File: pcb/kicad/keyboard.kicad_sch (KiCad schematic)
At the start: 0 parts

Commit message: pcb: make net-map the project schematic (keyboard.kicad_sch)
Rename net-map.kicad_sch -> keyboard.kicad_sch so it opens inside
keyboard.kicad_pro as the project's schematic (KiCad auto-associates by
filename; reference project confirms sheets:[] is fine). Refresh the
viewable render at pcb/kicad/net-map.png. Title marks it an overview,
not a netlist source — the board stays schematic-less.
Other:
- title: Atlas — Net Map -> Atlas — Net Map (overview, not netlist source)
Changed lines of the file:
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@@
 	(paper "A3")
 	(title_block
-		(title "Atlas — Net Map")
+		(title "Atlas — Net Map (overview, not netlist source)")
 		(date "2026-06-13")
-		(rev "v1")
+		(rev "v2")
 		(company "mwlabs")
 	)

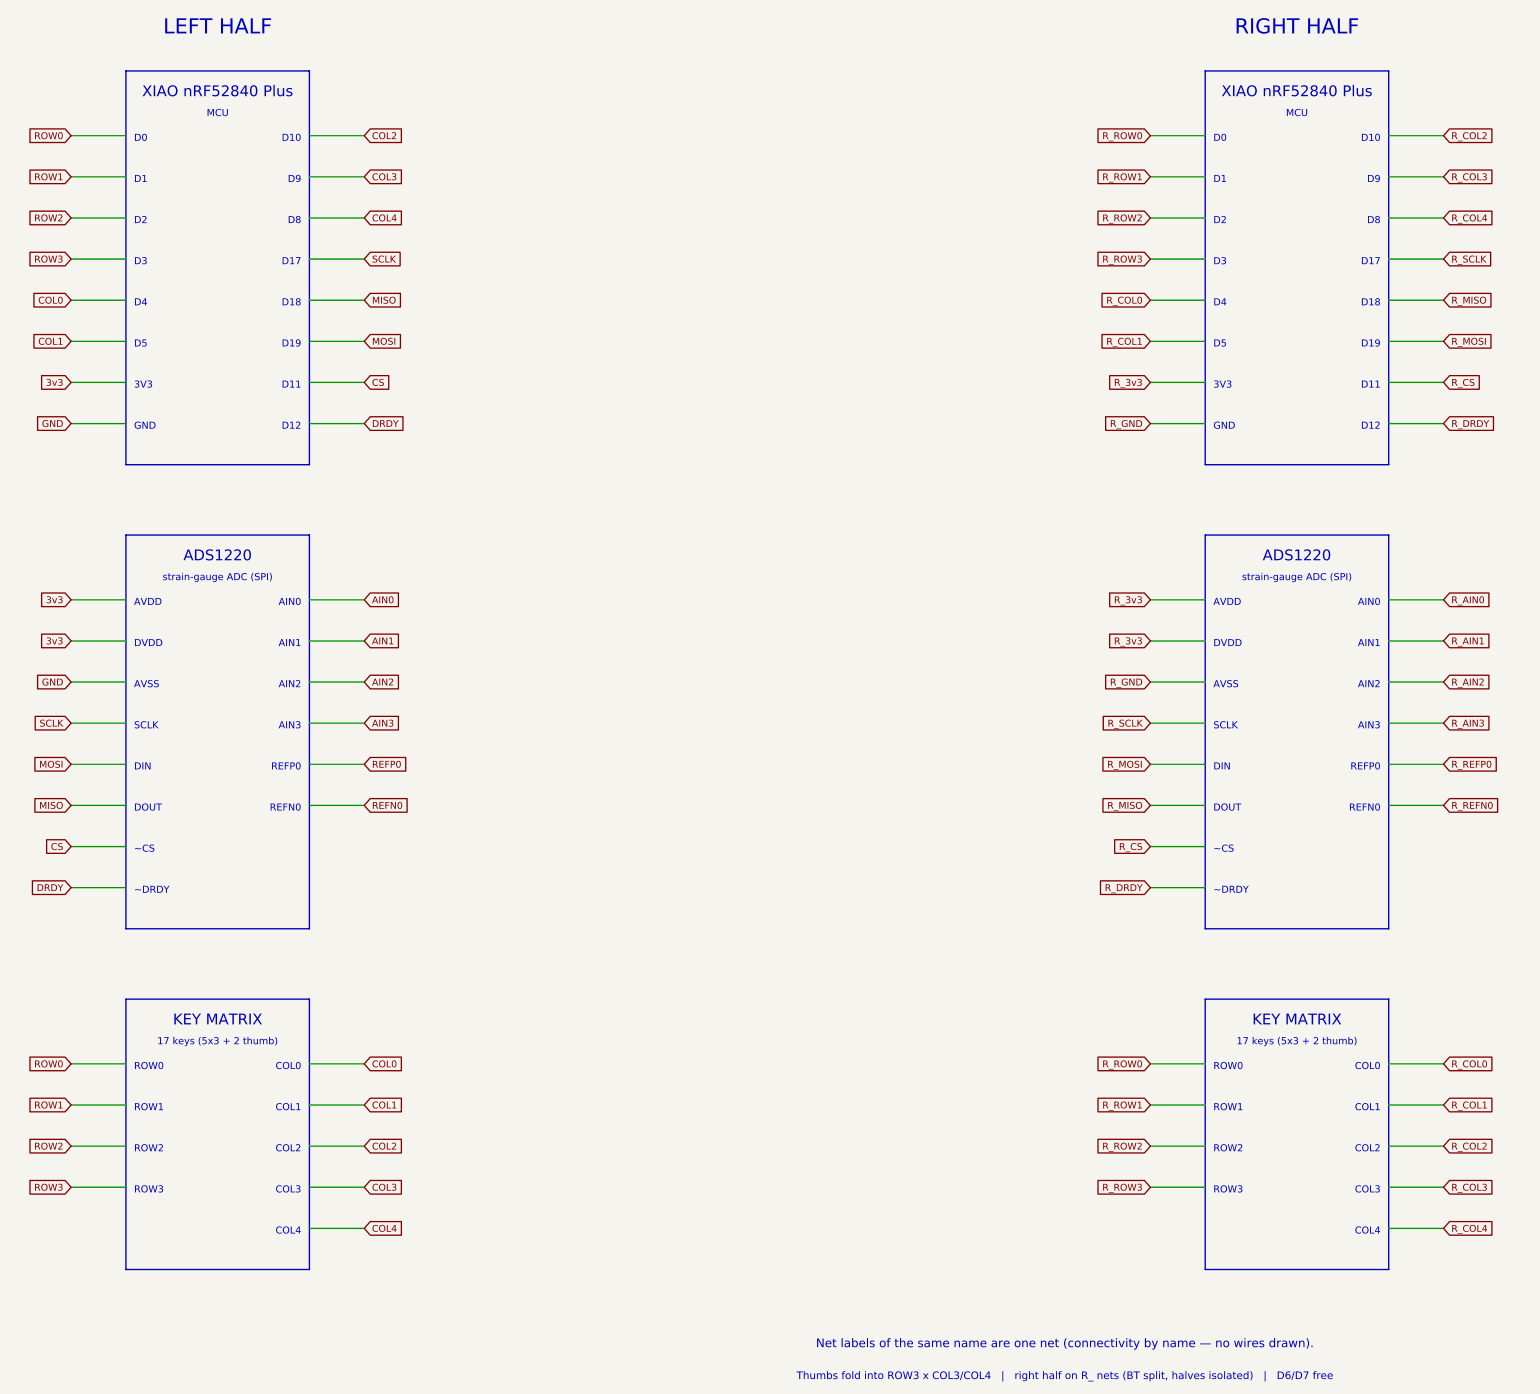
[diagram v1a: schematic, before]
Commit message: pcb(sch): add battery + on/off switch power path to net-map
Show the LiPo -> SPDT on/off slide (SSSS811101) -> XIAO BAT+ path per
half, and the XIAO BAT+/BAT- pins (the middle footprint pads). BAT-/GND
common; right half on R_ nets. Connectivity by net-label name.
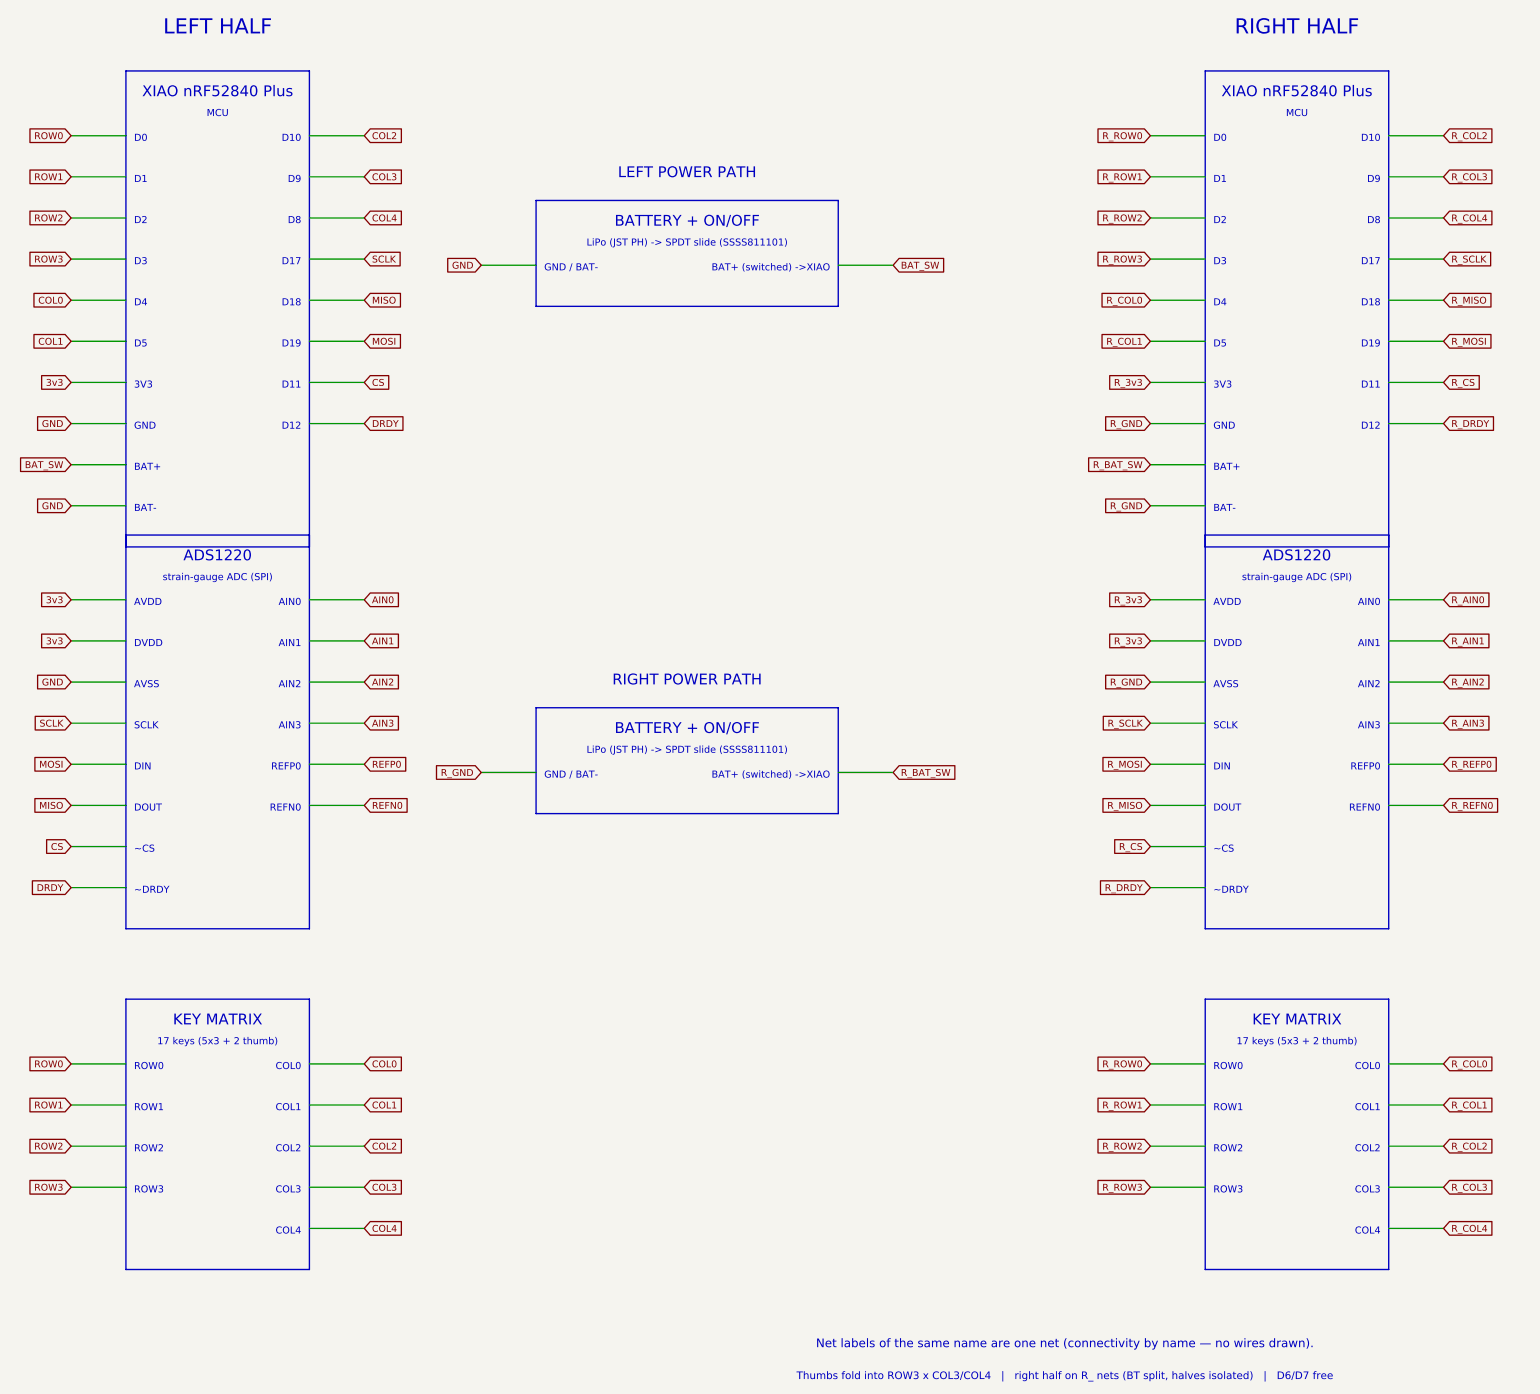
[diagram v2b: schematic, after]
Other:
- note added: "BAT+"
- note added: "BAT+ (switched) ->XIAO"
- note added: "BAT-"
- note added: "BATTERY + ON/OFF"
- note added: "GND / BAT-"
- note added: "LEFT POWER PATH"
- note added: "LiPo (JST PH) -> SPDT slide (SSSS811101)"
- note added: "RIGHT POWER PATH"
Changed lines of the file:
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@@
 	(text "LEFT HALF"(exclude_from_sim no)(at 53.0 24 0)
     (effects (font (size 2.8 2.8))))
-	(rectangle (start 36 32)(end 70 104.96000000000001)
+	(rectangle (start 36 32)(end 70 120.2)
     (stroke (width 0.254)(type default))(fill (type background)))
 	(text "XIAO nRF52840 Plus"(exclude_from_sim no)(at 53.0 36 0)
@@
 	(text "GND"(exclude_from_sim no)(at 37.5 97.94 0)
     (effects (font (size 1.3 1.3))(justify left)))
+	(wire (pts (xy 36 104.96000000000001)(xy 25.84 104.96000000000001))(stroke (width 0.152)(type default)))
+	(global_label "BAT_SW"(shape input)(at 25.84 104.96000000000001 0)
+    (effects (font (size 1.27 1.27))(justify right)))
+	(text "BAT+"(exclude_from_sim no)(at 37.5 105.56 0)
+    (effects (font (size 1.3 1.3))(justify left)))
+	(wire (pts (xy 36 112.58)(xy 25.84 112.58))(stroke (width 0.152)(type default)))
+	(global_label "GND"(shape input)(at 25.84 112.58 0)
+    (effects (font (size 1.27 1.27))(justify right)))
+	(text "BAT-"(exclude_from_sim no)(at 37.5 113.17999999999999 0)
+    (effects (font (size 1.3 1.3))(justify left)))
 	(wire (pts (xy 70 44.0)(xy 80.16 44.0))(stroke (width 0.152)(type default)))
 	(global_label "COL2"(shape input)(at 80.16 44.0 180)
@@
 	(text "RIGHT HALF"(exclude_from_sim no)(at 253.0 24 0)
     (effects (font (size 2.8 2.8))))
-	(rectangle (start 236 32)(end 270 104.96000000000001)
+	(rectangle (start 236 32)(end 270 120.2)
     (stroke (width 0.254)(type default))(fill (type background)))
 	(text "XIAO nRF52840 Plus"(exclude_from_sim no)(at 253.0 36 0)
@@
 	(text "GND"(exclude_from_sim no)(at 237.5 97.94 0)
     (effects (font (size 1.3 1.3))(justify left)))
+	(wire (pts (xy 236 104.96000000000001)(xy 225.84 104.96000000000001))(stroke (width 0.152)(type default)))
+	(global_label "R_BAT_SW"(shape input)(at 225.84 104.96000000000001 0)
+    (effects (font (size 1.27 1.27))(justify right)))
+	(text "BAT+"(exclude_from_sim no)(at 237.5 105.56 0)
+    (effects (font (size 1.3 1.3))(justify left)))
+	(wire (pts (xy 236 112.58)(xy 225.84 112.58))(stroke (width 0.152)(type default)))
+	(global_label "R_GND"(shape input)(at 225.84 112.58 0)
+    (effects (font (size 1.27 1.27))(justify right)))
+	(text "BAT-"(exclude_from_sim no)(at 237.5 113.17999999999999 0)
+    (effects (font (size 1.3 1.3))(justify left)))
 	(wire (pts (xy 270 44.0)(xy 280.16 44.0))(stroke (width 0.152)(type default)))
 	(global_label "R_COL2"(shape input)(at 280.16 44.0 180)
@@
 	(text "COL4"(exclude_from_sim no)(at 268.5 247.07999999999998 0)
     (effects (font (size 1.3 1.3))(justify right)))
+	(text "LEFT POWER PATH"(exclude_from_sim no)(at 140 51 0)
+    (effects (font (size 2.0 2.0))))
+	(rectangle (start 112 56)(end 168 75.62)
+    (stroke (width 0.254)(type default))(fill (type background)))
+	(text "BATTERY + ON/OFF"(exclude_from_sim no)(at 140.0 60 0)
+    (effects (font (size 2.0 2.0))))
+	(text "LiPo (JST PH) -> SPDT slide (SSSS811101)"(exclude_from_sim no)(at 140.0 64 0)
+    (effects (font (size 1.3 1.3))))
+	(wire (pts (xy 112 68.0)(xy 101.84 68.0))(stroke (width 0.152)(type default)))
+	(global_label "GND"(shape input)(at 101.84 68.0 0)
+    (effects (font (size 1.27 1.27))(justify right)))
+	(text "GND / BAT-"(exclude_from_sim no)(at 113.5 68.6 0)
+    (effects (font (size 1.3 1.3))(justify left)))
+	(wire (pts (xy 168 68.0)(xy 178.16 68.0))(stroke (width 0.152)(type default)))
+	(global_label "BAT_SW"(shape input)(at 178.16 68.0 180)
+    (effects (font (size 1.27 1.27))(justify left)))
+	(text "BAT+ (switched) ->XIAO"(exclude_from_sim no)(at 166.5 68.6 0)
+    (effects (font (size 1.3 1.3))(justify right)))
+	(text "RIGHT POWER PATH"(exclude_from_sim no)(at 140 145 0)
+    (effects (font (size 2.0 2.0))))
+	(rectangle (start 112 150)(end 168 169.62)
+    (stroke (width 0.254)(type default))(fill (type background)))
+	(text "BATTERY + ON/OFF"(exclude_from_sim no)(at 140.0 154 0)
+    (effects (font (size 2.0 2.0))))
+	(text "LiPo (JST PH) -> SPDT slide (SSSS811101)"(exclude_from_sim no)(at 140.0 158 0)
+    (effects (font (size 1.3 1.3))))
+	(wire (pts (xy 112 162.0)(xy 101.84 162.0))(stroke (width 0.152)(type default)))
+	(global_label "R_GND"(shape input)(at 101.84 162.0 0)
+    (effects (font (size 1.27 1.27))(justify right)))
+	(text "GND / BAT-"(exclude_from_sim no)(at 113.5 162.6 0)
+    (effects (font (size 1.3 1.3))(justify left)))
+	(wire (pts (xy 168 162.0)(xy 178.16 162.0))(stroke (width 0.152)(type default)))
+	(global_label "R_BAT_SW"(shape input)(at 178.16 162.0 180)
+    (effects (font (size 1.27 1.27))(justify left)))
+	(text "BAT+ (switched) ->XIAO"(exclude_from_sim no)(at 166.5 162.6 0)
+    (effects (font (size 1.3 1.3))(justify right)))
 	(text "Net labels of the same name are one net (connectivity by name — no wires drawn)."(exclude_from_sim no)(at 210 268 0)

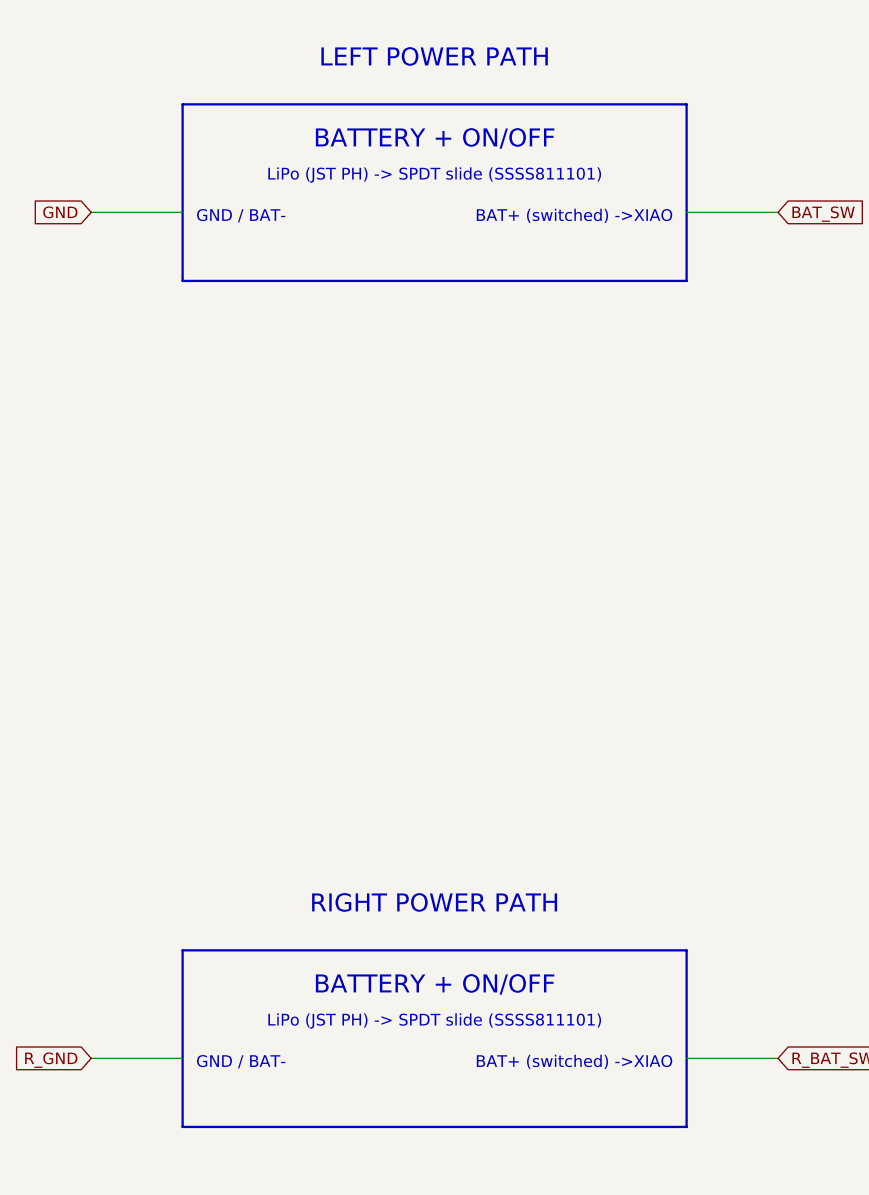
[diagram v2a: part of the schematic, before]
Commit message: pcb: battery uses soldered leads, not JST (update sch + doc)
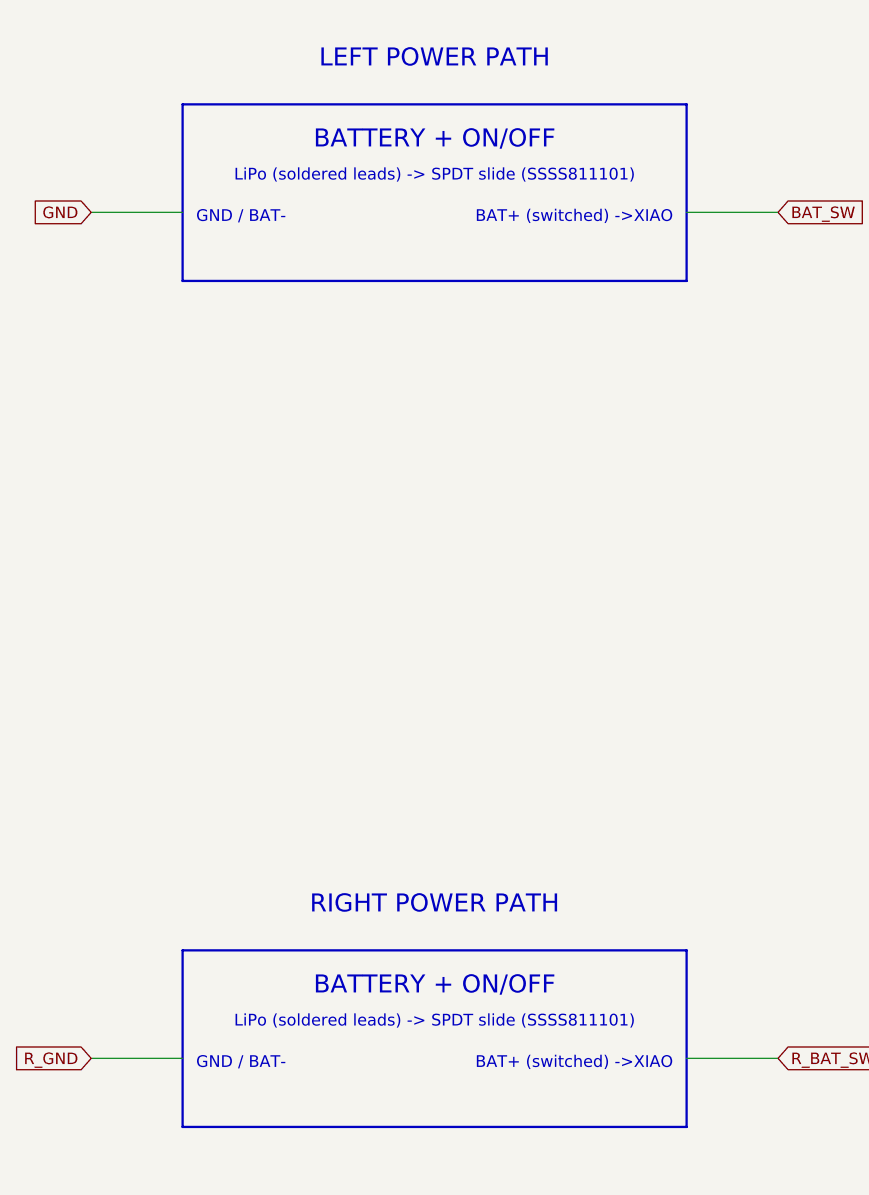
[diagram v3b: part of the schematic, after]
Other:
- note added: "LiPo (soldered leads) -> SPDT slide (SSSS811101)"
- note removed: "LiPo (JST PH) -> SPDT slide (SSSS811101)"
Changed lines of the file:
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@@
 	(text "BATTERY + ON/OFF"(exclude_from_sim no)(at 140.0 60 0)
     (effects (font (size 2.0 2.0))))
-	(text "LiPo (JST PH) -> SPDT slide (SSSS811101)"(exclude_from_sim no)(at 140.0 64 0)
+	(text "LiPo (soldered leads) -> SPDT slide (SSSS811101)"(exclude_from_sim no)(at 140.0 64 0)
     (effects (font (size 1.3 1.3))))
 	(wire (pts (xy 112 68.0)(xy 101.84 68.0))(stroke (width 0.152)(type default)))
@@
 	(text "BATTERY + ON/OFF"(exclude_from_sim no)(at 140.0 154 0)
     (effects (font (size 2.0 2.0))))
-	(text "LiPo (JST PH) -> SPDT slide (SSSS811101)"(exclude_from_sim no)(at 140.0 158 0)
+	(text "LiPo (soldered leads) -> SPDT slide (SSSS811101)"(exclude_from_sim no)(at 140.0 158 0)
     (effects (font (size 1.3 1.3))))
 	(wire (pts (xy 112 162.0)(xy 101.84 162.0))(stroke (width 0.152)(type default)))
